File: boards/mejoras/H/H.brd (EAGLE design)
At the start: 100 x 35 mm, 37 parts, among them IC1 PIC18F4455_TQFP

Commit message: small fixes to h
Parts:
- moved C3 5.39 mm to (66.5, 21.4)
- moved R1 1.15 mm to (66.8, 13.3)
- moved JP11 1.06 mm to (85.7, 8.22)
- moved R2 0.87 mm to (61.6, 13.5)
- moved R16 0.60 mm to (89.1, 7.08)
- moved LED1 0.46 mm to (21.4, 20.5)
- moved C4 0.43 mm to (48.0, 8.36)
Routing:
- net GND: track 416.7 -> 391.0 mm
- net CNY4: track 126.3 -> 117.0 mm
- net CNY3: track 79.0 -> 83.4 mm
- net VPOWER_SENSE: track 33.7 -> 30.6 mm, vias 3 -> 1
- net 5V: track 254.4 -> 251.5 mm
- net B1: track 37.9 -> 40.5 mm
- net PWM1: track 51.8 -> 53.2 mm
- net IN1B: track 32.3 -> 33.7 mm
- net CNY2: track 162.3 -> 163.4 mm
- net TX: track 34.2 -> 33.3 mm
- net CNY1: track 102.1 -> 102.8 mm
- net IN2B: track 16.0 -> 16.6 mm
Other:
- board text added: "C:/Users/Ariel/GitHub/Sumo-Robot-Programs-Database/boards/mejoras/I/ON.bmp"
- board text added: "C:/Users/Ariel/GitHub/Sumo-Robot-Programs-Database/boards/mejoras/I/chiari.bmp"

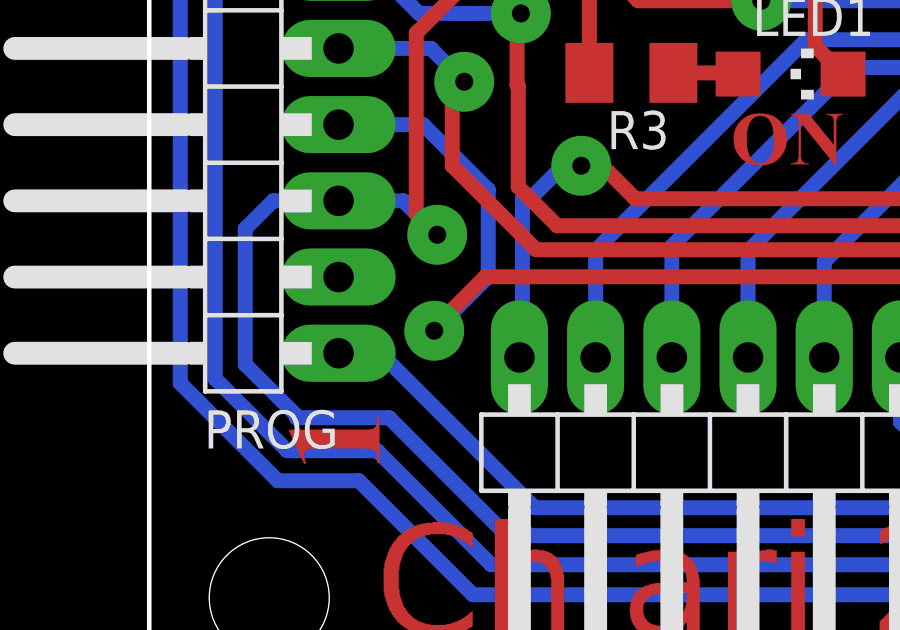
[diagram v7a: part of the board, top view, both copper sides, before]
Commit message: small fixes to g and i
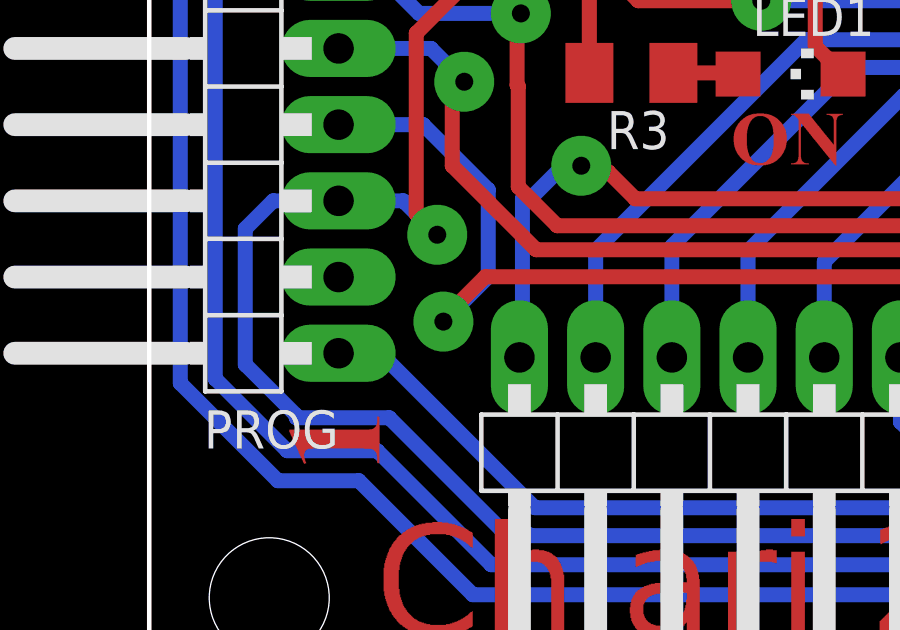
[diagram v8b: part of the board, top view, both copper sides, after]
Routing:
- net MCRL: track 46.7 -> 45.8 mm
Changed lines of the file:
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@@
 <wire x1="9.13" y1="18.77" x2="11.3" y2="16.6" width="0.5" layer="16"/>
 <wire x1="11.3" y1="16.6" x2="11.3" y2="13.7" width="0.5" layer="16"/>
-<wire x1="11.3" y1="13.7" x2="9.5" y2="11.9" width="0.5" layer="16"/>
-<via x="9.5" y="11.9" extent="1-16" drill="0.6" diameter="2"/>
+<wire x1="11.3" y1="13.7" x2="9.8048" y2="12.2048" width="0.5" layer="16"/>
+<via x="9.8048" y="12.2048" extent="1-16" drill="0.6" diameter="2"/>
 <wire x1="36" y1="13.7" x2="11.2" y2="13.7" width="0.5" layer="1"/>
-<wire x1="11.2" y1="13.7" x2="9.5" y2="12" width="0.5" layer="1"/>
-<wire x1="9.5" y1="11.9" x2="9.5" y2="12" width="0.5" layer="1"/>
+<wire x1="11.2" y1="13.7" x2="9.8048" y2="12.3048" width="0.5" layer="1"/>
+<wire x1="9.8048" y1="12.2048" x2="9.8048" y2="12.3048" width="0.5" layer="1"/>
 <wire x1="36.9" y1="14.6" x2="43.7" y2="14.6" width="0.5" layer="1"/>
 <wire x1="36" y1="13.7" x2="36.9" y2="14.6" width="0.5" layer="1"/>
